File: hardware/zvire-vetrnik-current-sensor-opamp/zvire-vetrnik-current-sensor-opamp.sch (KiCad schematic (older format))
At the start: 25 parts, among them J1 Conn_01x03, J2 Conn_Coaxial, J3 Conn_01x03, SW1 DP-06, U1 LMV358

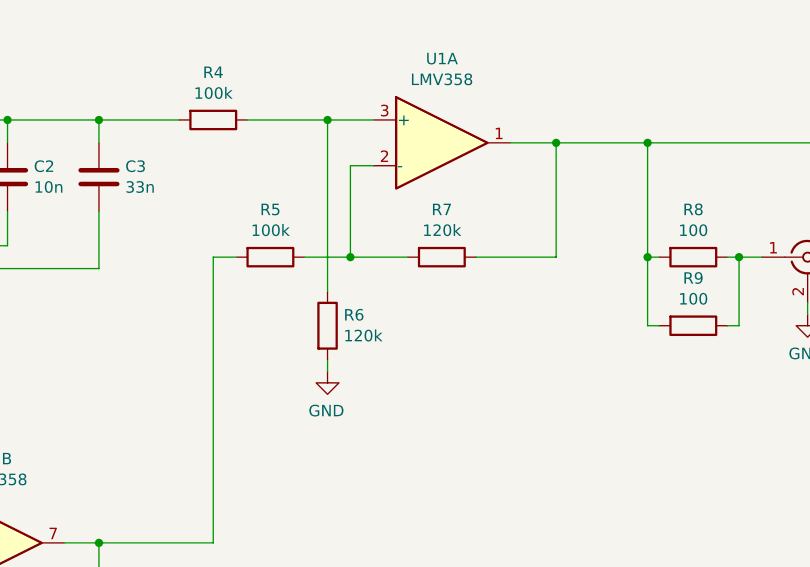
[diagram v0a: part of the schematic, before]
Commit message: [hardware] Resistor values in current-sensor-opamp
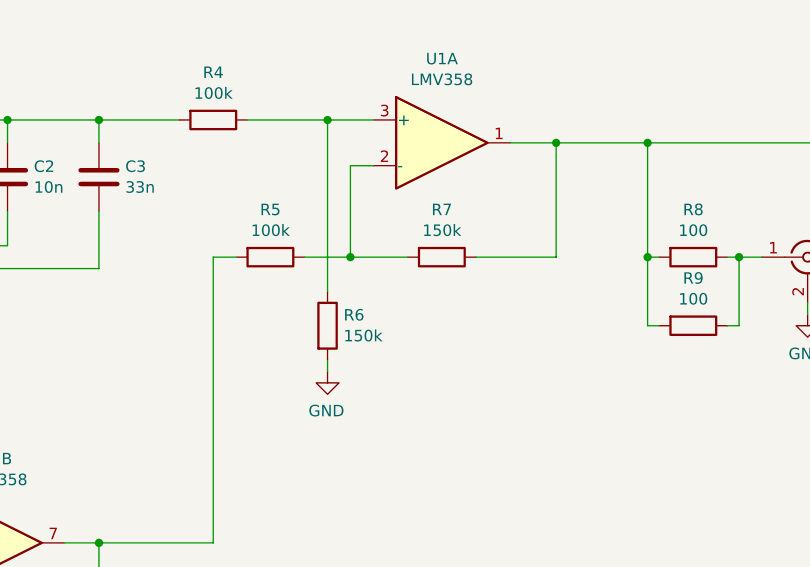
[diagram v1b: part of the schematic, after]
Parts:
- R6, R7: value 120k -> 150k
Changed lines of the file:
@@
 P 4000 3800
 F 0 "R6" H 4070 3846 50  0000 L CNN
-F 1 "120k" H 4070 3755 50  0000 L CNN
+F 1 "150k" H 4070 3755 50  0000 L CNN
 F 2 "Resistor_SMD:R_1206_3216Metric_Pad1.30x1.75mm_HandSolder" V 3930 3800 50  0001 C CNN
 F 3 "~" H 4000 3800 50  0001 C CNN
@@
 P 4500 3500
 F 0 "R7" V 4293 3500 50  0000 C CNN
-F 1 "120k" V 4384 3500 50  0000 C CNN
+F 1 "150k" V 4384 3500 50  0000 C CNN
 F 2 "Resistor_SMD:R_1206_3216Metric_Pad1.30x1.75mm_HandSolder" V 4430 3500 50  0001 C CNN
 F 3 "~" H 4500 3500 50  0001 C CNN

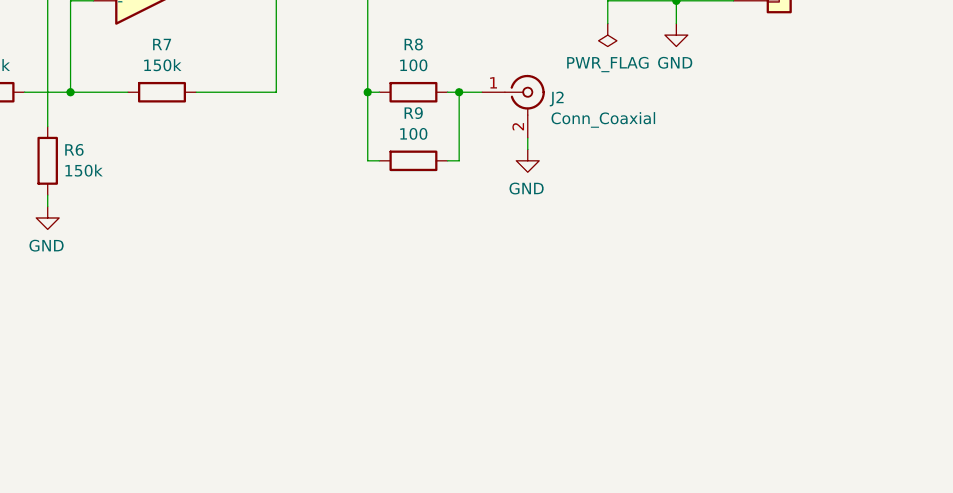
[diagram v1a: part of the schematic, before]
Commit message: Add current-sensor-opamp notes
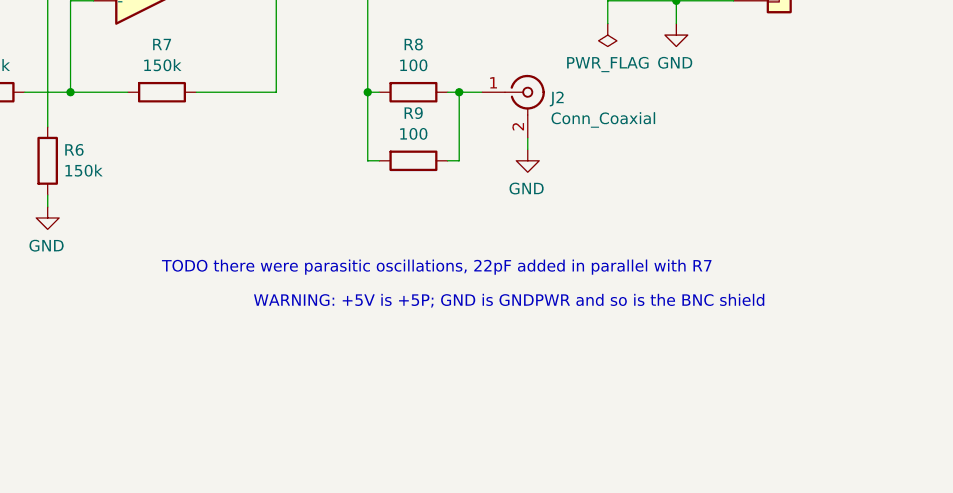
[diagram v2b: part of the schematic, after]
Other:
- note added: "TODO there were parasitic oscillations, 22pF added in parallel with R7"
- note added: "WARNING: +5V is +5P; GND is GNDPWR and so is the BNC shield"
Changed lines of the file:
@@
 Wire Wire Line
 	2150 3650 2000 3650
+Text Notes 4900 4450 0    50   ~ 0
+WARNING: +5V is +5P; GND is GNDPWR and so is the BNC shield
+Text Notes 4500 4300 0    50   ~ 0
+TODO there were parasitic oscillations, 22pF added in parallel with R7
 $EndSCHEMATC
